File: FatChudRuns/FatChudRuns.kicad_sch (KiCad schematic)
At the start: 2 parts, among them U1 STM32F107RBTx, U2 DP83848I

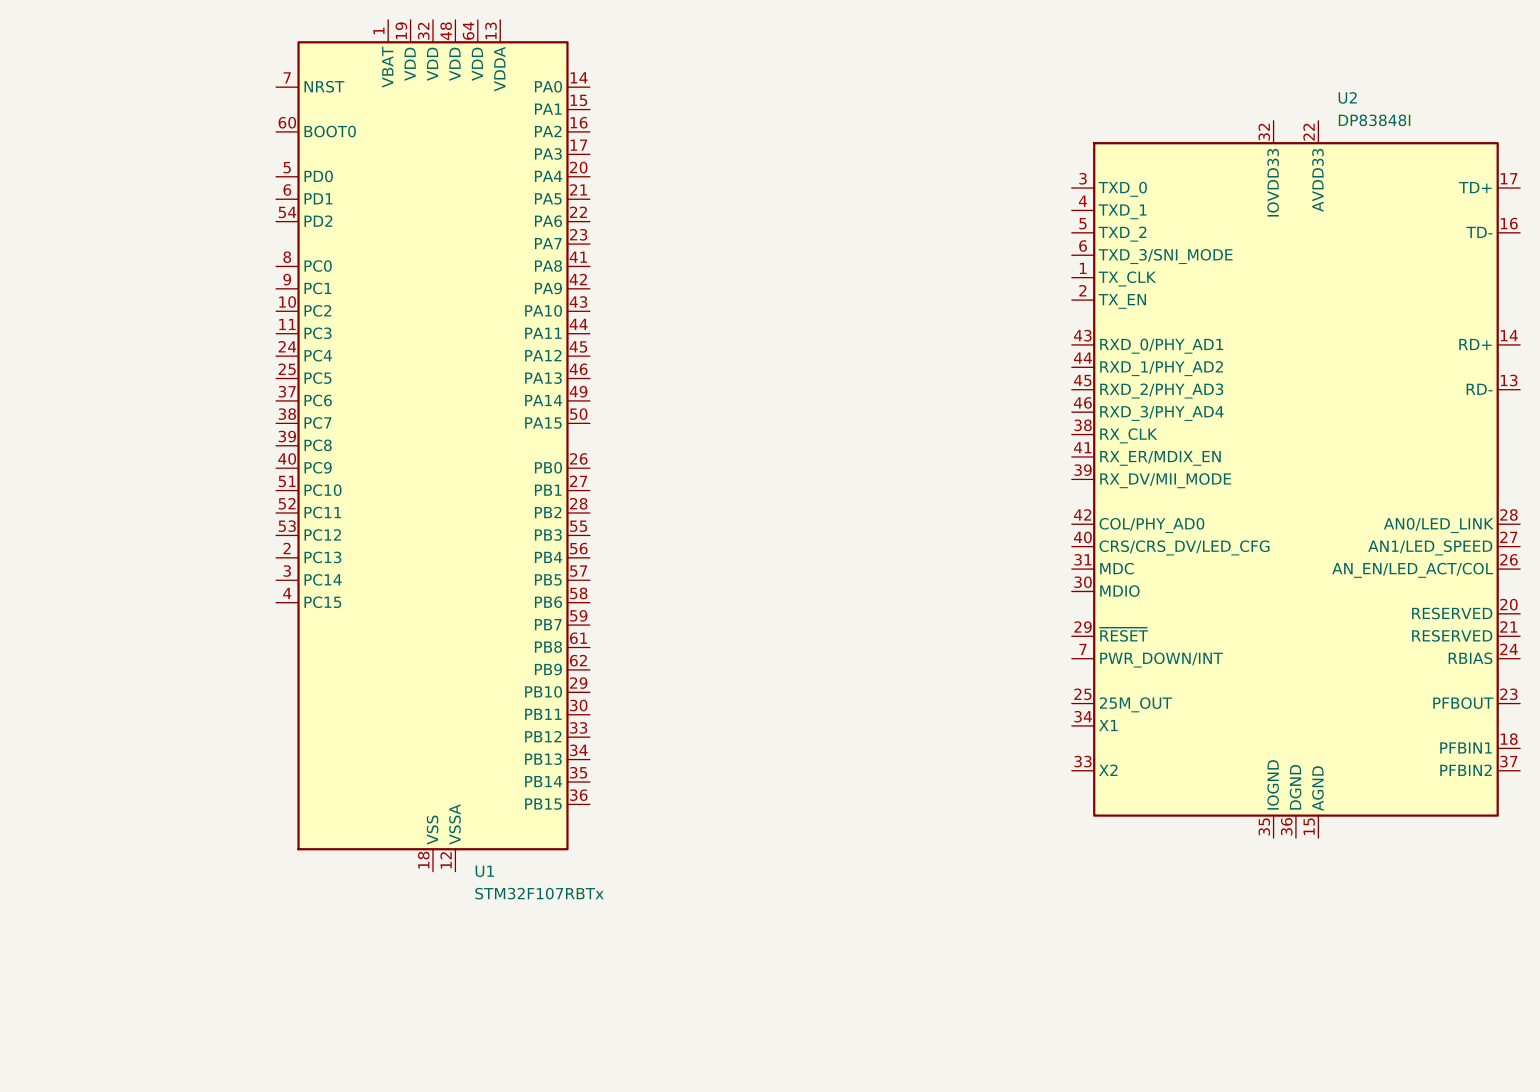
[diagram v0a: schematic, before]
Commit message: added switch and dip switch for mcu, decoup caps. new sheets for power and eth phy
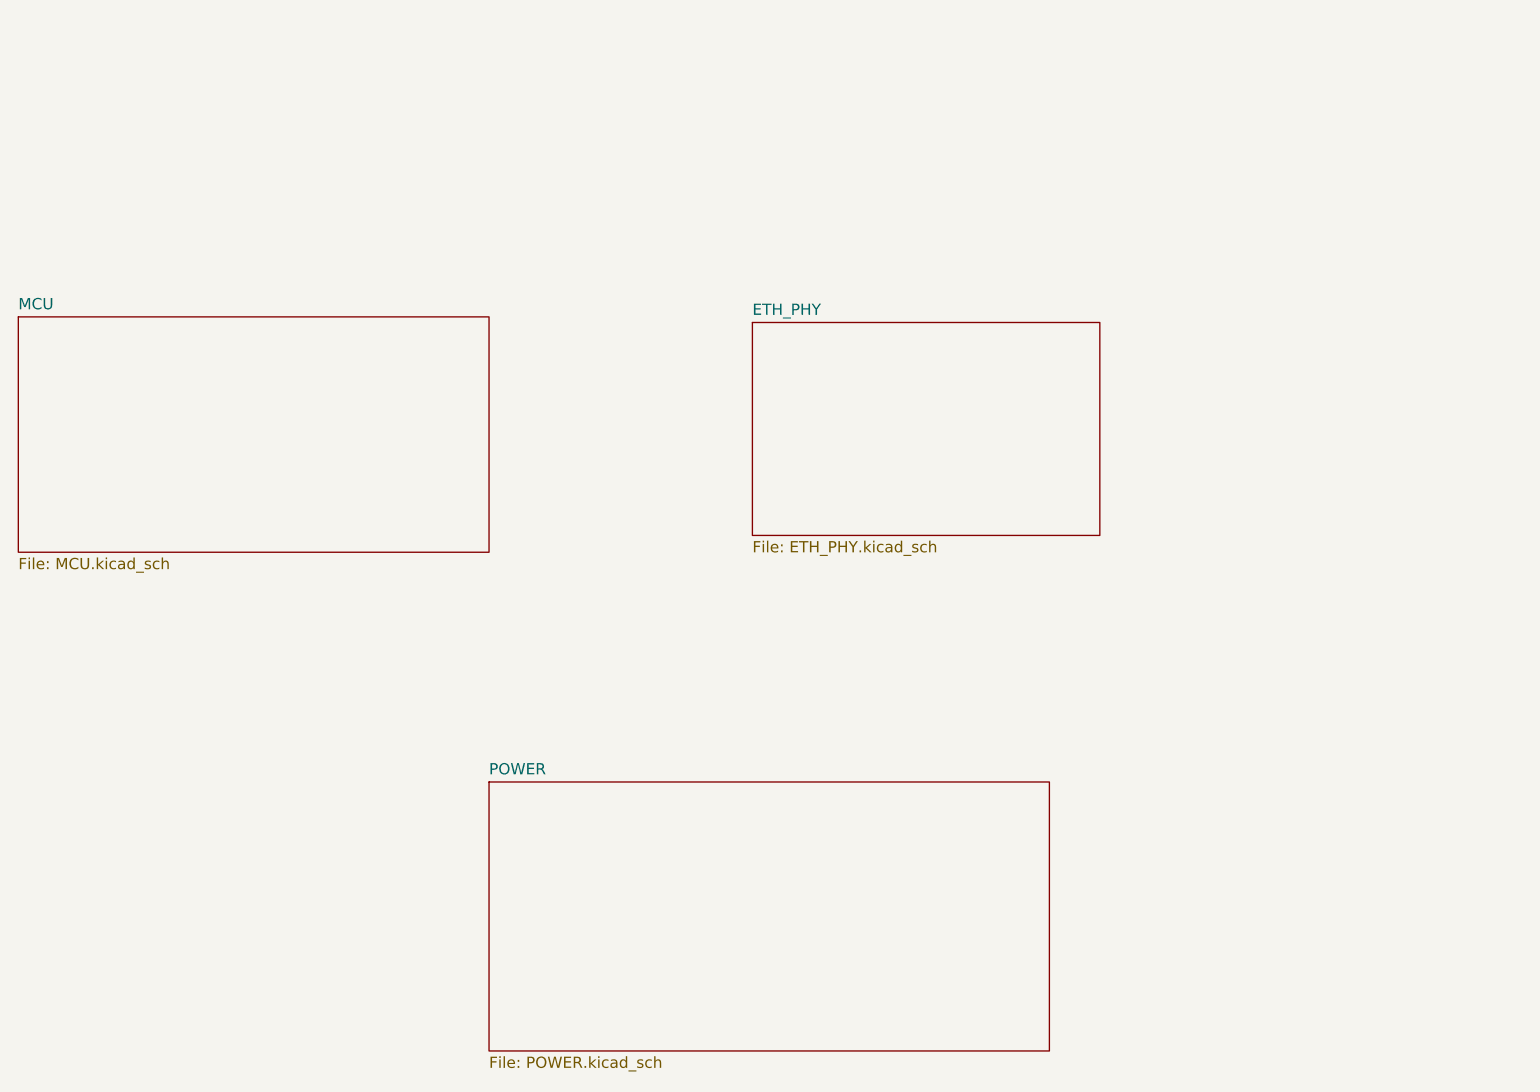
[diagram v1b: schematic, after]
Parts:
- removed U1: STM32F107RBTx, Package_QFP:LQFP-64_10x10mm_P0.5mm, symbol MCU_ST_STM32F1:STM32F107RBTx
- removed U2: DP83848I, Package_QFP:LQFP-48_7x7mm_P0.5mm, symbol Interface_Ethernet:DP83848I
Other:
- added sheet ETH_PHY (ETH_PHY.kicad_sch)
- added sheet MCU (MCU.kicad_sch)
- added sheet POWER (POWER.kicad_sch)

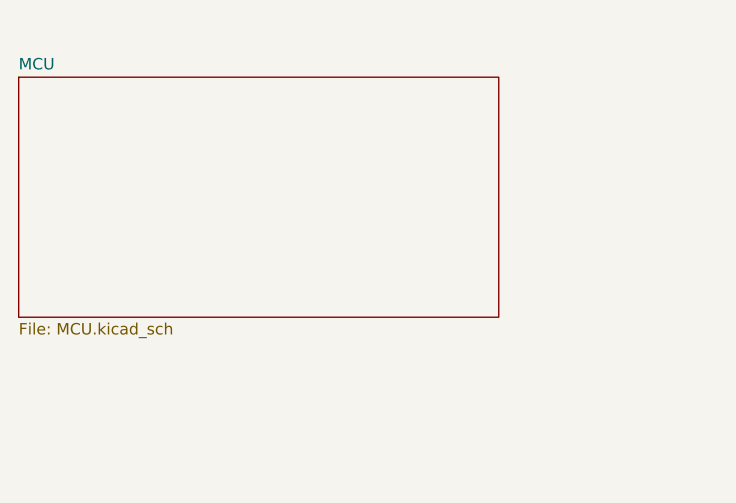
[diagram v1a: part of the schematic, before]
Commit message: selected rj45 w/ mag, fixed filtering for power, added snippets of layout recs
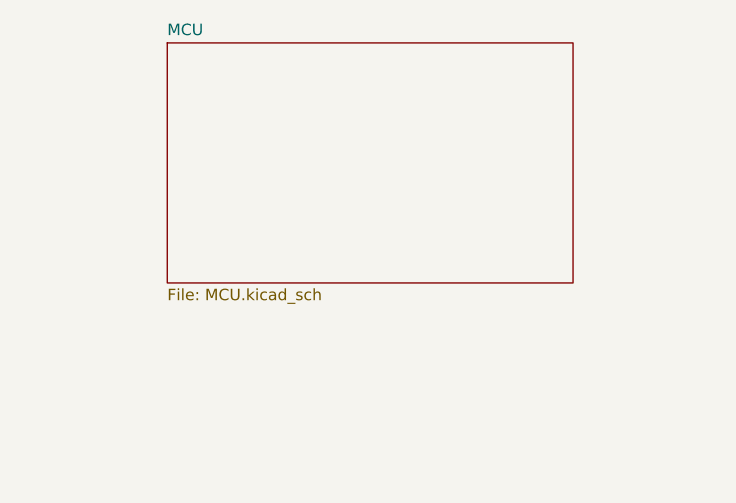
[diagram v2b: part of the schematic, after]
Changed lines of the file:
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@@
 	)
 	(sheet
-		(at 48.26 59.055)
-		(size 53.34 26.67)
+		(at 64.77 55.245)
+		(size 45.085 26.67)
 		(exclude_from_sim no)
 		(in_bom yes)
@@
 		)
 		(property "Sheetname" "MCU"
-			(at 48.26 58.3434 0)
+			(at 64.77 54.5334 0)
 			(effects
 				(font
@@
 		)
 		(property "Sheetfile" "MCU.kicad_sch"
-			(at 48.26 86.3096 0)
+			(at 64.77 82.4996 0)
 			(effects
 				(font

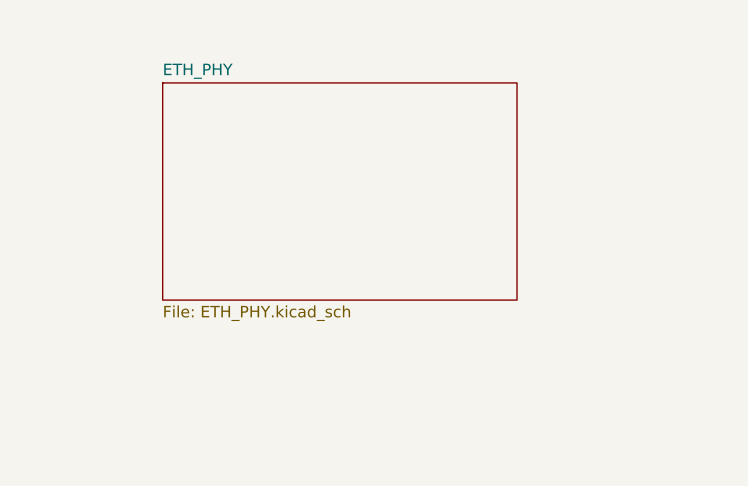
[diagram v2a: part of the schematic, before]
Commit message: added debugger and nucleo ref sch
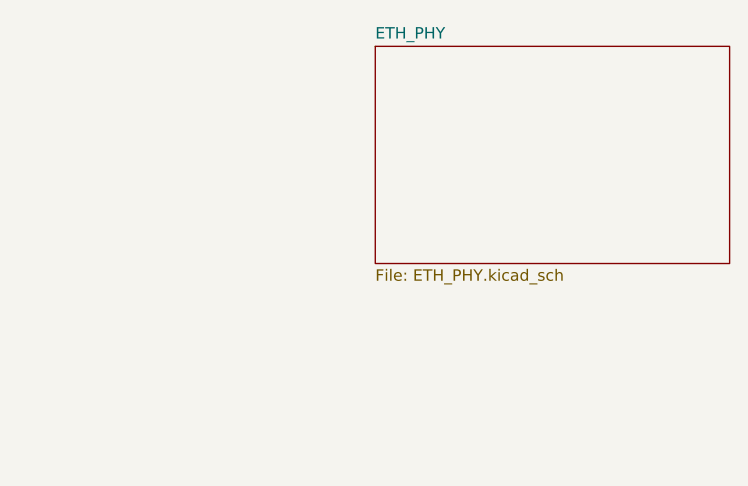
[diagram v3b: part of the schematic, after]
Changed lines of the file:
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@@
 	)
 	(sheet
-		(at 131.445 59.69)
+		(at 155.067 55.626)
 		(size 39.37 24.13)
 		(exclude_from_sim no)
@@
 		)
 		(property "Sheetname" "ETH_PHY"
-			(at 131.445 58.9784 0)
+			(at 155.067 54.9144 0)
 			(effects
 				(font
@@
 		)
 		(property "Sheetfile" "ETH_PHY.kicad_sch"
-			(at 131.445 84.4046 0)
+			(at 155.067 80.3406 0)
 			(effects
 				(font

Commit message: updated 3d model footprint for Rj45 (created new library)
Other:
- title: STM32 Value Line Discovery - Shiled board -> FatChudRuns
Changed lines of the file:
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@@
 	(paper "A4")
 	(title_block
-		(title "STM32 Value Line Discovery - Shiled board")
+		(title "FatChudRuns")
 		(date "20 oct 2012")
 		(rev "1.0")
